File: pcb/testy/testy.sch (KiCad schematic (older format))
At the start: 68 parts, among them SW0:0 SW_Push, SW0:1 SW_Push, SW0:2 SW_Push, SW0:3 SW_Push, SW0:4 SW_Push, SW0:5 SW_Push, SW1:0 SW_Push, SW1:1 SW_Push, SW1:2 SW_Push, SW1:3 SW_Push, SW1:4 SW_Push, SW1:5 SW_Push, SW2:0 SW_Push, SW2:1 SW_Push, SW2:2 SW_Push, SW2:3 SW_Push, SW2:4 SW_Push, SW2:5 SW_Push, SW3:0 SW_Push, SW3:1 SW_Push, SW3:2 SW_Push, SW3:3 SW_Push, SW3:4 SW_Push, SW3:5 SW_Push, SW3:6 SW_Push, SW4:1 SW_Push, SW4:2 SW_Push, SW4:3 SW_Push, SW4:4 SW_Push, SW4:6 SW_Push, U1 ProMicro

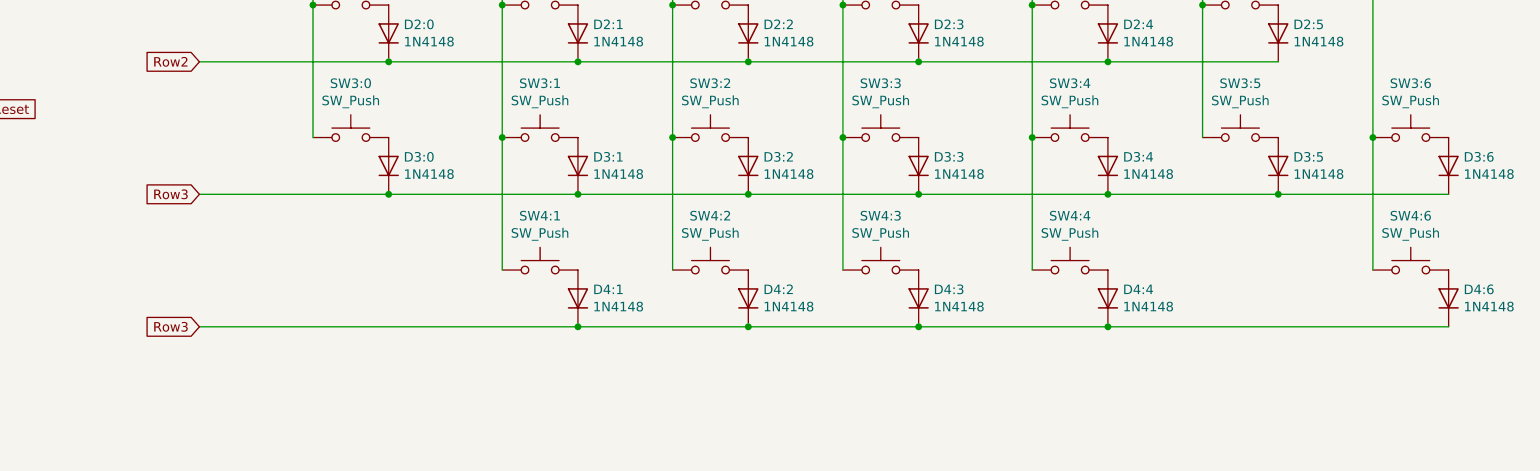
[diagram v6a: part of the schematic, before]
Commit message: feat: add all footprint refs, update netlist, do some wiring
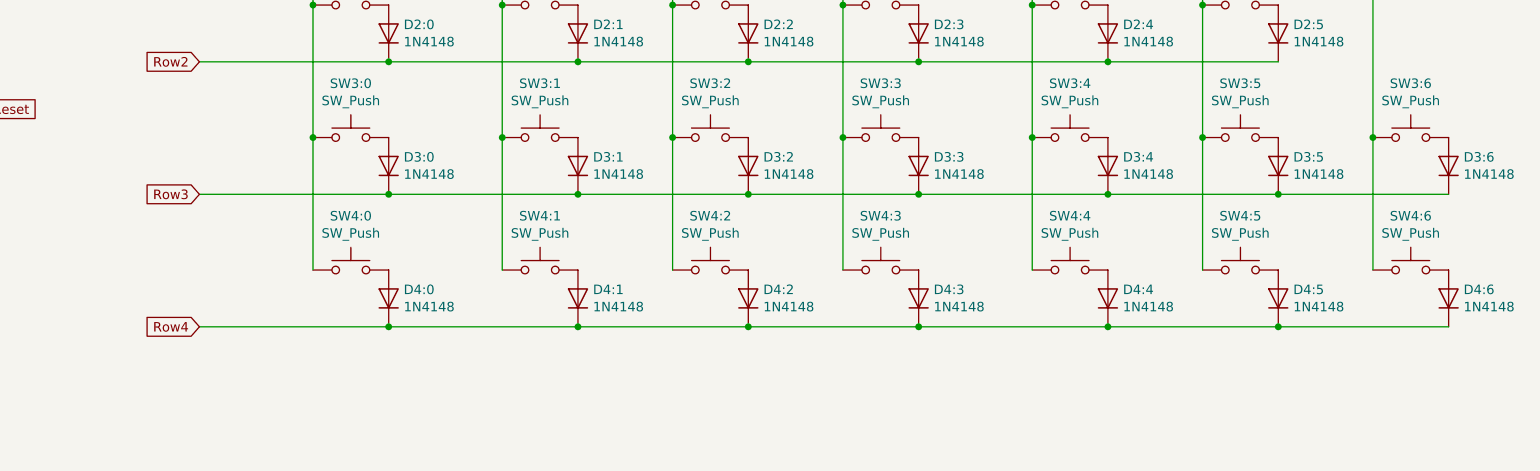
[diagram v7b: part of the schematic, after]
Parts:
- added D4:0, D4:5: 1N4148, Diode_THT:D_DO-35_SOD27_P7.62mm_Horizontal, symbol Diode:1N4148
- added SW4:0, SW4:5: SW_Push, footprints:kailh-socket-and-choc-solder-reversible, symbol Switch:SW_Push
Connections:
- net Col0: now also SW4:0.1
- net Col5: now also SW4:5.1
- net Row3: no longer D4:1.1 (K), D4:2.1 (K), D4:3.1 (K), D4:4.1 (K), D4:6.1 (K)
- net Row4: now also D4:1.1 (K), D4:2.1 (K), D4:3.1 (K), D4:4.1 (K), D4:6.1 (K), D4:0.1 (K), D4:5.1 (K)
- new net: D4:0.2 (A), SW4:0.2
- new net: D4:5.2 (A), SW4:5.2
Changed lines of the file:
@@
 Connection ~ 6550 4650
 Text GLabel 3650 4650 0    50   Input ~ 0
-Row3
+Row4
 $Comp
 L Switch:SW_Push SW4:4
@@
 	9850 950  9850 3650
 Wire Wire Line
-	8450 4650 10250 4650
-Wire Wire Line
-	3650 4650 5650 4650
+	8450 4650 9350 4650
 Connection ~ 8450 2550
 Wire Wire Line
@@
 Wire Wire Line
 	900  4200 900  4250
+$Comp
+L Switch:SW_Push SW4:0
+U 1 1 5DCA6DFA
+P 4450 4350
+F 0 "SW4:0" H 4450 4635 50  0000 C CNN
+F 1 "SW_Push" H 4450 4544 50  0000 C CNN
+F 2 "footprints:kailh-socket-and-choc-solder-reversible" H 4450 4550 50  0001 C CNN
+F 3 "~" H 4450 4550 50  0001 C CNN
+	1    4450 4350
+	1    0    0    -1
+$EndComp
+Wire Wire Line
+	4250 3650 4250 4350
+$Comp
+L Diode:1N4148 D4:0
+U 1 1 5DCA6E05
+P 4650 4500
+F 0 "D4:0" V 4696 4421 50  0000 R CNN
+F 1 "1N4148" V 4605 4421 50  0000 R CNN
+F 2 "Diode_THT:D_DO-35_SOD27_P7.62mm_Horizontal" H 4650 4325 50  0001 C CNN
+F 3 "https://assets.nexperia.com/documents/data-sheet/1N4148_1N4448.pdf" H 4650 4500 50  0001 C CNN
+	1    4650 4500
+	0    -1   -1   0
+$EndComp
+Wire Wire Line
+	3650 4650 4650 4650
+Connection ~ 4250 3650
+Connection ~ 4650 4650
+Wire Wire Line
+	4650 4650 5650 4650
+$Comp
+L Switch:SW_Push SW4:5
+U 1 1 5DCF66B6
+P 9150 4350
+F 0 "SW4:5" H 9150 4635 50  0000 C CNN
+F 1 "SW_Push" H 9150 4544 50  0000 C CNN
+F 2 "footprints:kailh-socket-and-choc-solder-reversible" H 9150 4550 50  0001 C CNN
+F 3 "~" H 9150 4550 50  0001 C CNN
+	1    9150 4350
+	1    0    0    -1
+$EndComp
+Wire Wire Line
+	8950 3650 8950 4350
+$Comp
+L Diode:1N4148 D4:5
+U 1 1 5DCF66C1
+P 9350 4500
+F 0 "D4:5" V 9396 4421 50  0000 R CNN
+F 1 "1N4148" V 9305 4421 50  0000 R CNN
+F 2 "Diode_THT:D_DO-35_SOD27_P7.62mm_Horizontal" H 9350 4325 50  0001 C CNN
+F 3 "https://assets.nexperia.com/documents/data-sheet/1N4148_1N4448.pdf" H 9350 4500 50  0001 C CNN
+	1    9350 4500
+	0    -1   -1   0
+$EndComp
+Connection ~ 8950 3650
+Connection ~ 9350 4650
+Wire Wire Line
+	9350 4650 10250 4650
 $EndSCHEMATC

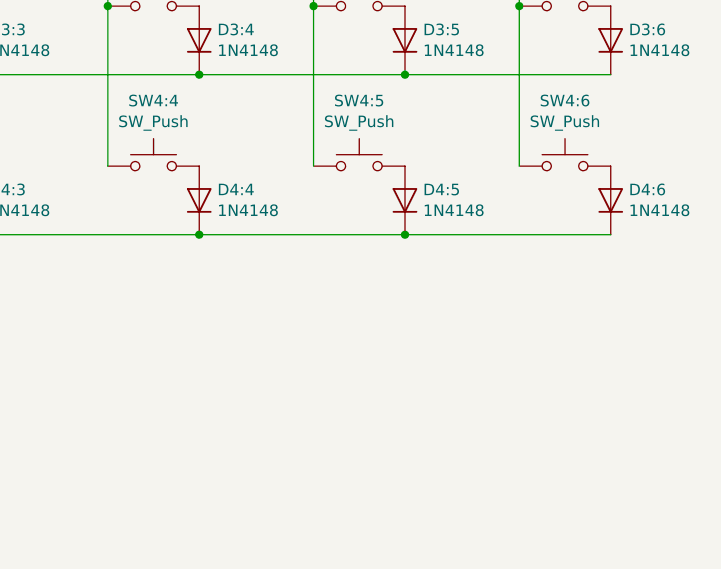
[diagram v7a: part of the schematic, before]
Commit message: feat: wire up edge connectors
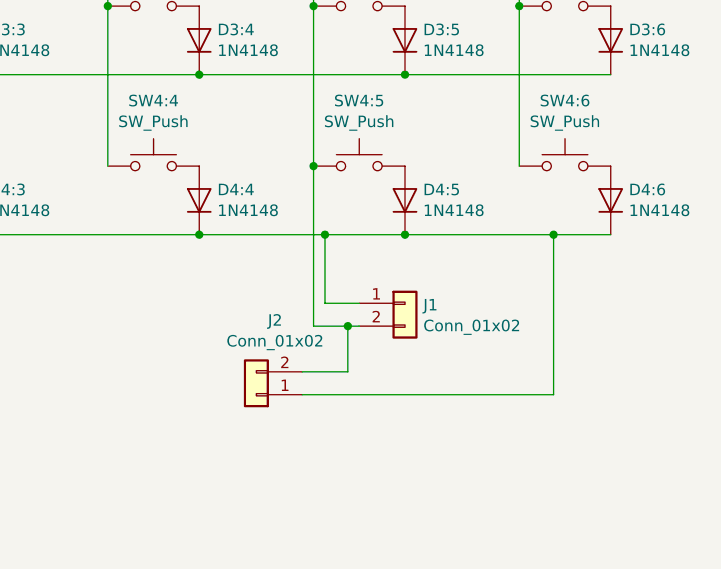
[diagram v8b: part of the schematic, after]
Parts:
- added J1, J2: Conn_01x02, footprints:edge-connector, symbol Connector_Generic:Conn_01x02
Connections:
- net Col5: now also J1.2 (Pin_2), J2.2 (Pin_2)
- net Row4: now also J1.1 (Pin_1), J2.1 (Pin_1)
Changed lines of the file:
@@
 	9850 950  9850 3650
 Wire Wire Line
-	8450 4650 9350 4650
+	8450 4650 9000 4650
 Connection ~ 8450 2550
 Wire Wire Line
@@
 Connection ~ 9350 4650
 Wire Wire Line
-	9350 4650 10250 4650
+	9350 4650 10000 4650
+$Comp
+L Connector_Generic:Conn_01x02 J1
+U 1 1 5DC944CA
+P 9350 4950
+F 0 "J1" H 9430 4942 50  0000 L CNN
+F 1 "Conn_01x02" H 9430 4851 50  0000 L CNN
+F 2 "footprints:edge-connector" H 9350 4950 50  0001 C CNN
+F 3 "~" H 9350 4950 50  0001 C CNN
+	1    9350 4950
+	1    0    0    -1
+$EndComp
+Wire Wire Line
+	8950 4350 8950 5050
+Wire Wire Line
+	8950 5050 9100 5050
+Connection ~ 8950 4350
+Wire Wire Line
+	9000 4650 9000 4950
+Wire Wire Line
+	9000 4950 9150 4950
+Connection ~ 9000 4650
+Wire Wire Line
+	9000 4650 9350 4650
+$Comp
+L Connector_Generic:Conn_01x02 J2
+U 1 1 5DC9EDA4
+P 8700 5350
+F 0 "J2" H 8618 5025 50  0000 C CNN
+F 1 "Conn_01x02" H 8618 5116 50  0000 C CNN
+F 2 "footprints:edge-connector" H 8700 5350 50  0001 C CNN
+F 3 "~" H 8700 5350 50  0001 C CNN
+	1    8700 5350
+	-1   0    0    1
+$EndComp
+Wire Wire Line
+	9100 5050 9100 5250
+Wire Wire Line
+	9100 5250 8900 5250
+Connection ~ 9100 5050
+Wire Wire Line
+	9100 5050 9150 5050
+Wire Wire Line
+	10000 4650 10000 5350
+Wire Wire Line
+	10000 5350 8900 5350
+Connection ~ 10000 4650
+Wire Wire Line
+	10000 4650 10250 4650
 $EndSCHEMATC
